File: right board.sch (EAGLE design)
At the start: 29 parts, among them IC1 LM555D, IC2 LM555D

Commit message: added switches to light board
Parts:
- added D2, D3, D6, D7: SRP100, diode:SRP100
- added U$1, U$2: JS_SERIES_SLIDESWITCCH, slide switch:JS_SERIES_SLIDESWITCCH
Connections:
- removed net N$13: C3.1, IC2.THR, VR2.S
- removed net N$17: VR2.E
- new net B_BLINK: IC1.GND, IC1.Q, NMOS.S, R3.2, U$1.OUT1
- new net D_BLINK: IC2.GND, IC2.Q, NMOS1.S, R6.2, U$2.OUT1
- new net N$1: D2.A, VR2.E
- new net N$9: D3.C, VR2.A
- net BLINK: now also U$1.IN; no longer IC1.GND, IC1.Q, NMOS.S, R3.2
- net B_OUT: now also U$1.OUT2
- net DRIVE: now also U$2.IN; no longer IC2.GND, IC2.Q, NMOS1.S, R6.2
- net D_OUT: now also U$2.OUT2
- net N$12: now also C1.1, IC1.R, IC1.THR, VR1.S; no longer IC2.DIS
- net N$14: now also D3.A, IC2.DIS; no longer VR2.A
- net N$18: now also D2.C
- net N$2: now also C3.1, IC2.R, IC2.THR, VR2.S; no longer IC1.DIS
- net N$3: now also D7.C, VR1.A; no longer C1.1, IC1.THR, VR1.S
- net N$4: now also D7.A, IC1.DIS; no longer VR1.A
- net N$5: now also D6.A
- net N$7: now also D6.C

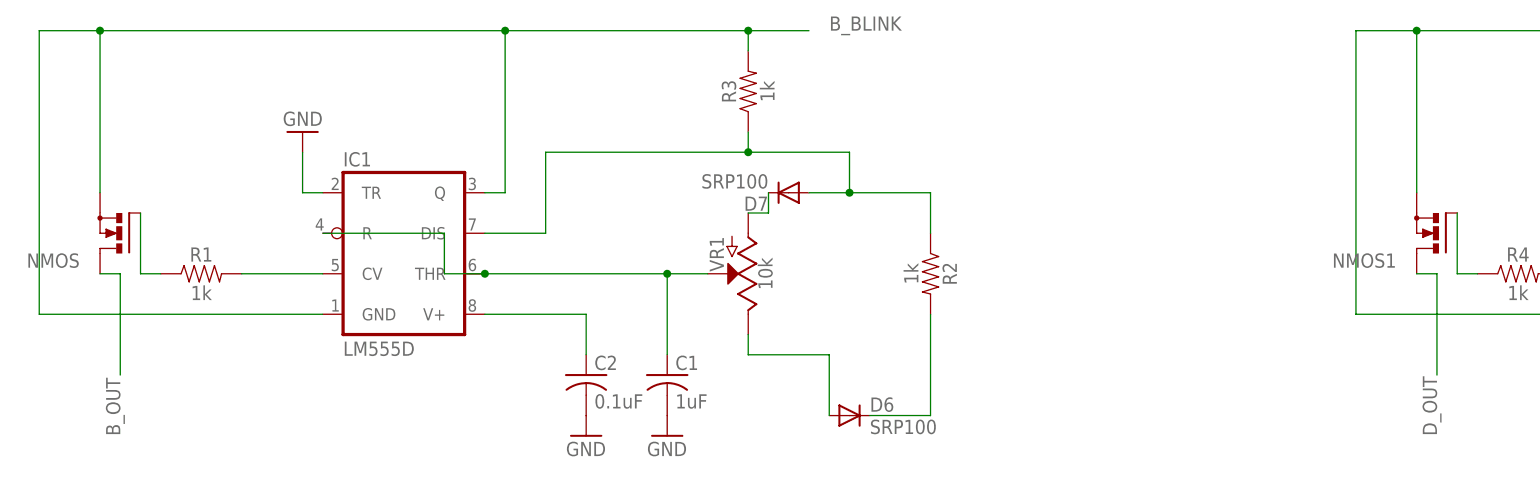
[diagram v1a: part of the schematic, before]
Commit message: updated mosfets on lights
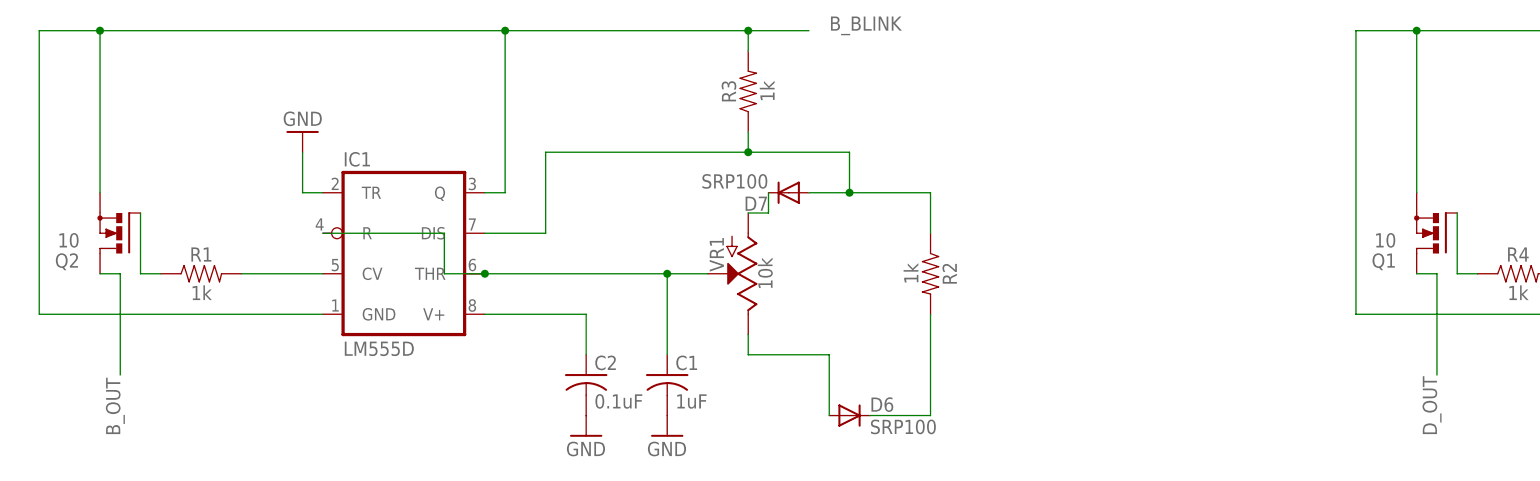
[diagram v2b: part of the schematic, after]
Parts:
- removed NMOS, NMOS1: (no value), transistor-power:N-MOSFET-SO8S
- added Q1, Q2: 10, transistor-power:PMOSFET_NTO220BV
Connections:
- net B_BLINK: now also Q2.S; no longer NMOS.S
- net B_OUT: now also Q2.D; no longer NMOS.D
- net D_BLINK: now also Q1.S; no longer NMOS1.S
- net D_OUT: now also Q1.D; no longer NMOS1.D
- net N$19: now also Q1.G; no longer NMOS1.G
- net N$8: now also Q2.G; no longer NMOS.G
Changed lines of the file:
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@@
 <part name="C2" library="E-P-008-R1.2" deviceset="C-US" device="025-024X044" value="0.1uF"/>
 <part name="GND1" library="E-P-008-R1.2" deviceset="GND" device=""/>
-<part name="NMOS" library="transistor-power" library_urn="urn:adsk.eagle:library:400" deviceset="N-MOSFET-SO8" device="S" package3d_urn="urn:adsk.eagle:package:29505/2"/>
 <part name="GND2" library="E-P-008-R1.2" deviceset="GND" device=""/>
 <part name="GND4" library="E-P-008-R1.2" deviceset="GND" device=""/>
@@
 <part name="C4" library="E-P-008-R1.2" deviceset="C-US" device="025-024X044" value="0.1uF"/>
 <part name="GND5" library="E-P-008-R1.2" deviceset="GND" device=""/>
-<part name="NMOS1" library="transistor-power" library_urn="urn:adsk.eagle:library:400" deviceset="N-MOSFET-SO8" device="S" package3d_urn="urn:adsk.eagle:package:29505/2"/>
 <part name="GND6" library="E-P-008-R1.2" deviceset="GND" device=""/>
 <part name="GND8" library="E-P-008-R1.2" deviceset="GND" device=""/>
@@
 <part name="D6" library="diode" library_urn="urn:adsk.eagle:library:210" deviceset="SRP100" device="" package3d_urn="urn:adsk.eagle:package:43336/1"/>
 <part name="D7" library="diode" library_urn="urn:adsk.eagle:library:210" deviceset="SRP100" device="" package3d_urn="urn:adsk.eagle:package:43336/1"/>
+<part name="Q1" library="transistor-power" library_urn="urn:adsk.eagle:library:400" deviceset="PMOSFET_N" device="TO220BV" package3d_urn="urn:adsk.eagle:package:29484/1" value="10"/>
+<part name="Q2" library="transistor-power" library_urn="urn:adsk.eagle:library:400" deviceset="PMOSFET_N" device="TO220BV" package3d_urn="urn:adsk.eagle:package:29484/1" value="10"/>
 </parts>
 <sheets>
@@
 <instance part="C2" gate="G$1" x="-66.04" y="25.4"/>
 <instance part="GND1" gate="1" x="-55.88" y="17.78"/>
-<instance part="NMOS" gate="G$1" x="-124.46" y="43.18" rot="R180"/>
 <instance part="GND2" gate="1" x="-66.04" y="17.78"/>
 <instance part="GND4" gate="1" x="-101.6" y="55.88" rot="R180"/>
@@
 <instance part="C4" gate="G$1" x="99.06" y="25.4"/>
 <instance part="GND5" gate="1" x="109.22" y="17.78"/>
-<instance part="NMOS1" gate="G$1" x="40.64" y="43.18" rot="R180"/>
 <instance part="GND6" gate="1" x="99.06" y="17.78"/>
 <instance part="GND8" gate="1" x="63.5" y="55.88" rot="R180"/>
@@
 <instance part="D6" gate="1" x="-33.02" y="20.32"/>
 <instance part="D7" gate="1" x="-40.64" y="48.26" rot="R180"/>
+<instance part="Q1" gate="G$1" x="40.64" y="43.18" rot="R180"/>
+<instance part="Q2" gate="G$1" x="-124.46" y="43.18" rot="R180"/>
 </instances>
 <busses>
@@
 <segment>
 <pinref part="R1" gate="G$1" pin="1"/>
-<pinref part="NMOS" gate="G$1" pin="G"/>
 <wire x1="-119.38" y1="38.1" x2="-121.92" y2="38.1" width="0.1524" layer="91"/>
 <wire x1="-121.92" y1="38.1" x2="-121.92" y2="45.72" width="0.1524" layer="91"/>
+<pinref part="Q2" gate="G$1" pin="G"/>
 </segment>
 </net>
@@
 <segment>
 <pinref part="R4" gate="G$1" pin="1"/>
-<pinref part="NMOS1" gate="G$1" pin="G"/>
 <wire x1="45.72" y1="38.1" x2="43.18" y2="38.1" width="0.1524" layer="91"/>
 <wire x1="43.18" y1="38.1" x2="43.18" y2="45.72" width="0.1524" layer="91"/>
+<pinref part="Q1" gate="G$1" pin="G"/>
 </segment>
 </net>
@@
 </segment>
 <segment>
-<pinref part="NMOS" gate="G$1" pin="D"/>
 <wire x1="-127" y1="38.1" x2="-124.46" y2="38.1" width="0.1524" layer="91"/>
 <wire x1="-124.46" y1="38.1" x2="-124.46" y2="25.4" width="0.1524" layer="91"/>
 <label x="-124.46" y="17.78" size="1.778" layer="95" rot="R90"/>
+<pinref part="Q2" gate="G$1" pin="D"/>
 </segment>
 <segment>
@@
 </segment>
 <segment>
-<pinref part="NMOS1" gate="G$1" pin="D"/>
 <wire x1="38.1" y1="38.1" x2="40.64" y2="38.1" width="0.1524" layer="91"/>
 <wire x1="40.64" y1="38.1" x2="40.64" y2="25.4" width="0.1524" layer="91"/>
 <label x="40.64" y="17.78" size="1.778" layer="95" rot="R90"/>
+<pinref part="Q1" gate="G$1" pin="D"/>
 </segment>
 <segment>
@@
 <wire x1="66.04" y1="33.02" x2="30.48" y2="33.02" width="0.1524" layer="91"/>
 <wire x1="30.48" y1="33.02" x2="30.48" y2="68.58" width="0.1524" layer="91"/>
-<pinref part="NMOS1" gate="G$1" pin="S"/>
 <wire x1="38.1" y1="48.26" x2="38.1" y2="68.58" width="0.1524" layer="91"/>
 <junction x="38.1" y="68.58"/>
@@
 <wire x1="119.38" y1="68.58" x2="119.38" y2="66.04" width="0.1524" layer="91"/>
 <junction x="119.38" y="68.58"/>
+<pinref part="Q1" gate="G$1" pin="S"/>
 </segment>
 </net>
@@
 <wire x1="-99.06" y1="33.02" x2="-134.62" y2="33.02" width="0.1524" layer="91"/>
 <wire x1="-134.62" y1="33.02" x2="-134.62" y2="68.58" width="0.1524" layer="91"/>
-<pinref part="NMOS" gate="G$1" pin="S"/>
 <wire x1="-127" y1="48.26" x2="-127" y2="68.58" width="0.1524" layer="91"/>
 <junction x="-127" y="68.58"/>
@@
 <wire x1="-45.72" y1="68.58" x2="-45.72" y2="66.04" width="0.1524" layer="91"/>
 <junction x="-45.72" y="68.58"/>
-</segment>
-</net>
+<pinref part="Q2" gate="G$1" pin="S"/>
+</segment>
+</net>

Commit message: Gerbers generated
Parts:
- removed C1, C3: 1uF, E-P-008-R1.2:C-US025-024X044
- removed C2, C4: 0.1uF, E-P-008-R1.2:C-US025-024X044
- removed D2, D3, D6, D7: SRP100, diode:SRP100
- removed LED30, LED31, LED32, LED33, LED34, LED35, LED36, LED37, LED38: (no value), E-P-008-R1.2:LED
- removed R1, R2, R3, R4, R5, R6: 1k, SparkFun-Resistors:1KOHM-0603-1/10W-1%
- removed VR1, VR2: 10k, SparkFun-Resistors:POTENTIOMETER-PTH-9MM-1/20W-20%
- added C5, C7: 1.0uF, SparkFun-Capacitors-extra:1.0UF-25V-+80/-20(0805)"
- added C6, C8: 0.1uF, SparkFun-Capacitors-extra:0.1UF-25V(+80/-20%)(0603)
- added D1, D10, D11, D12, D13, D14, D15, D16, D17, D18, D19, D20, D21, D22, D23, D24, D25, D26, D27, D28, D4, D5, D8, D9: (no value), SparkFun-LED:LED5MM
- added D29, D30, D31, D32: (no value), SparkFun-DiscreteSemi:DIODESMA
- added R10, R11, R13, R14, R9: 1k, SparkFun-Resistors:0.22OHM-1/4W-1%(0805)
- added R12: 30, SparkFun-Resistors:0.22OHM-1/4W-1%(0805)
- added U$3: 10k, SparkFun-Resistors:10K_LINEAR_POT_SMD
- added U$4: 10K_LINEAR_POT_SMD, SparkFun-Resistors:10K_LINEAR_POT_SMD
- R7: value (none) -> 30; device resistor:R-US_0204/2V -> SparkFun-Resistors:0.22OHM-1/4W-1%(0805)
- R8: value (none) -> 1k; device resistor:R-US_0204/5 -> SparkFun-Resistors:0.22OHM-1/4W-1%(0805)
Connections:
- removed net N$37: LED30.C, LED31.A
- removed net N$38: LED31.C, LED32.A
- removed net N$39: LED32.C, LED33.A
- removed net N$40: LED34.C, LED35.A
- removed net N$41: LED35.C, LED36.A
- removed net N$42: LED36.C, LED37.A
- removed net N$43: LED30.A, R8.2
- removed net N$44: LED34.A, R7.1
- removed net N$48: LED37.C, LED38.A
- new net N$11: D1.C, D10.A, D11.A, D12.A, D4.C, D5.C, D8.C, D9.A
- new net N$13: D1.A, D4.A, D5.A, D8.A, R12.2
- new net N$17: D17.C, D18.C, D19.C, D20.C, D21.A, D22.A, D23.A, D24.A
- new net N$20: D21.C, D22.C, D23.C, D24.C, D25.A, D26.A, D27.A, D28.A
- new net N$21: D10.C, D11.C, D12.C, D13.A, D14.A, D15.A, D16.A, D9.C
- new net N$22: D17.A, D18.A, D19.A, D20.A, R7.2
- net B_BLINK: now also R13.2; no longer R3.2
- net B_OUT: now also R12.1; no longer R8.1
- net D_BLINK: now also R9.1; no longer R6.2
- net D_OUT: now also R7.1; no longer R7.2
- net GND: now also C5.2, C6.2, C7.2, C8.2, D13.C, D14.C, D15.C, D16.C, D25.C, D26.C, D27.C, D28.C; no longer C1.2, C2.2, C3.2, C4.2, LED33.C, LED38.C
- net N$1: now also D29.A, U$4.E; no longer D2.A, VR2.E
- net N$10: now also R14.1; no longer R1.2
- net N$12: now also C7.1, U$3.S; no longer C1.1, VR1.S
- net N$14: now also D30.A, R8.1, R9.2; no longer D3.A, R5.1, R6.1
- net N$15: now also C6.1; no longer C4.1
- net N$16: now also R10.2; no longer R4.2
- net N$18: now also D29.C, R8.2; no longer D2.C, R5.2
- net N$19: now also R10.1; no longer R4.1
- net N$2: now also C5.1, U$4.S; no longer C3.1, VR2.S
- net N$3: now also D32.C, U$3.A; no longer D7.C, VR1.A
- net N$4: now also D32.A, R11.2, R13.1; no longer D7.A, R2.1, R3.1
- net N$5: now also D31.A, U$3.E; no longer D6.A, VR1.E
- net N$6: now also C8.1; no longer C2.1
- net N$7: now also D31.C, R11.1; no longer D6.C, R2.2
- net N$8: now also R14.2; no longer R1.1
- net N$9: now also D30.C, U$4.A; no longer D3.C, VR2.A
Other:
- moved on the sheet: R7, R8

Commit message: all gerbers generated
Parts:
- added H1, H2, H3, H4: STAND-OFF, SparkFun-Electromechanical:STAND-OFF
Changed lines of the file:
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@@
 <part name="C7" library="SparkFun-Capacitors-extra" deviceset="1.0UF-25V-+80/-20(0805)" device="&quot;" value="1.0uF"/>
 <part name="C8" library="SparkFun-Capacitors-extra" deviceset="0.1UF-25V(+80/-20%)(0603)" device="" value="0.1uF"/>
+<part name="H1" library="SparkFun-Electromechanical" deviceset="STAND-OFF" device=""/>
+<part name="H2" library="SparkFun-Electromechanical" deviceset="STAND-OFF" device=""/>
+<part name="H3" library="SparkFun-Electromechanical" deviceset="STAND-OFF" device=""/>
+<part name="H4" library="SparkFun-Electromechanical" deviceset="STAND-OFF" device=""/>
 </parts>
 <sheets>
@@
 <instance part="C7" gate="G$1" x="-55.88" y="22.86"/>
 <instance part="C8" gate="G$1" x="-66.04" y="22.86"/>
+<instance part="H1" gate="G$1" x="71.12" y="86.36"/>
+<instance part="H2" gate="G$1" x="76.2" y="86.36"/>
+<instance part="H3" gate="G$1" x="81.28" y="86.36"/>
+<instance part="H4" gate="G$1" x="86.36" y="86.36"/>
 </instances>
 <busses>

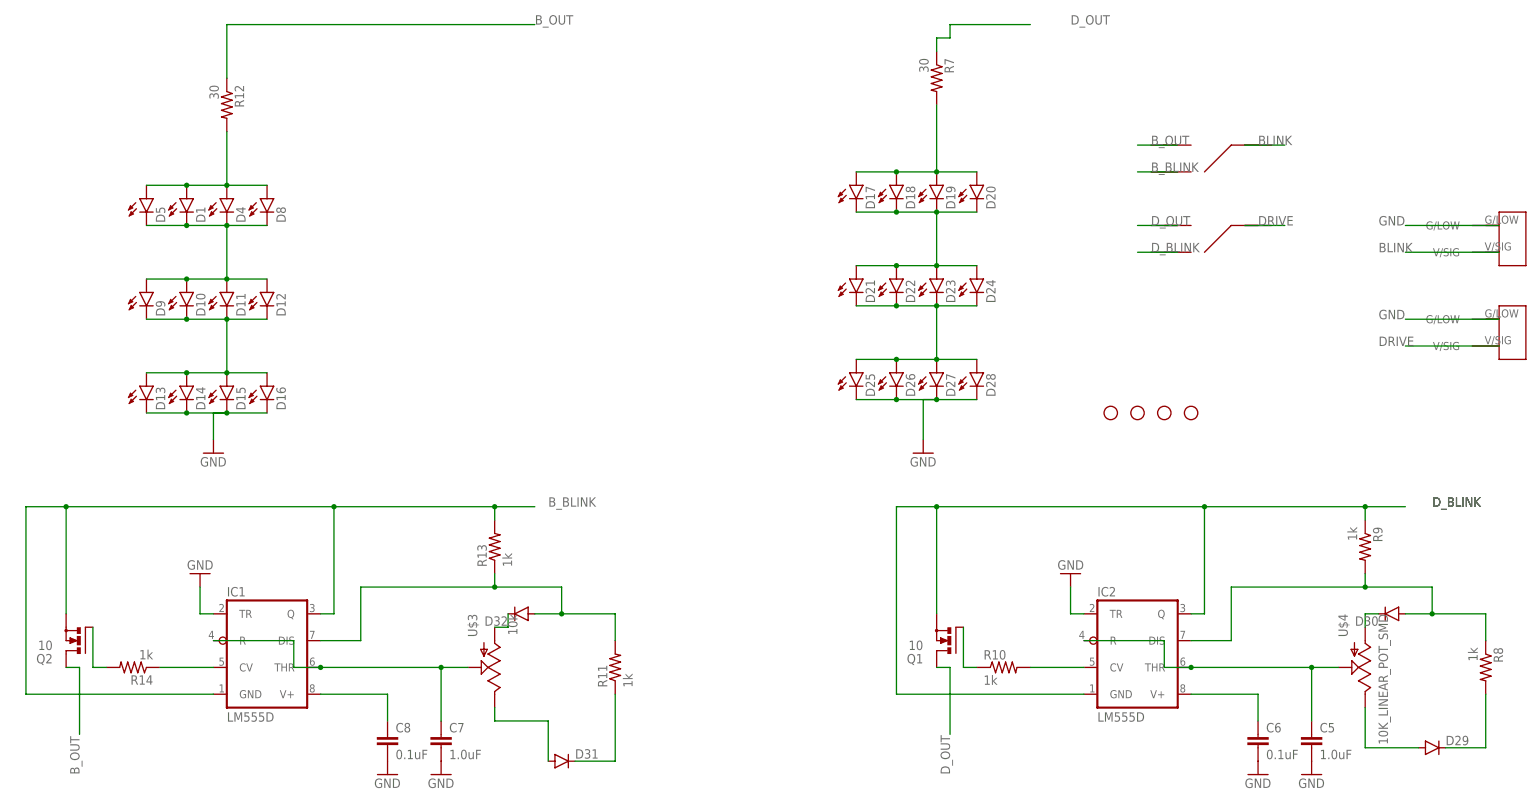
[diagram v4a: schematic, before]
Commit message: added reverse polairity protection
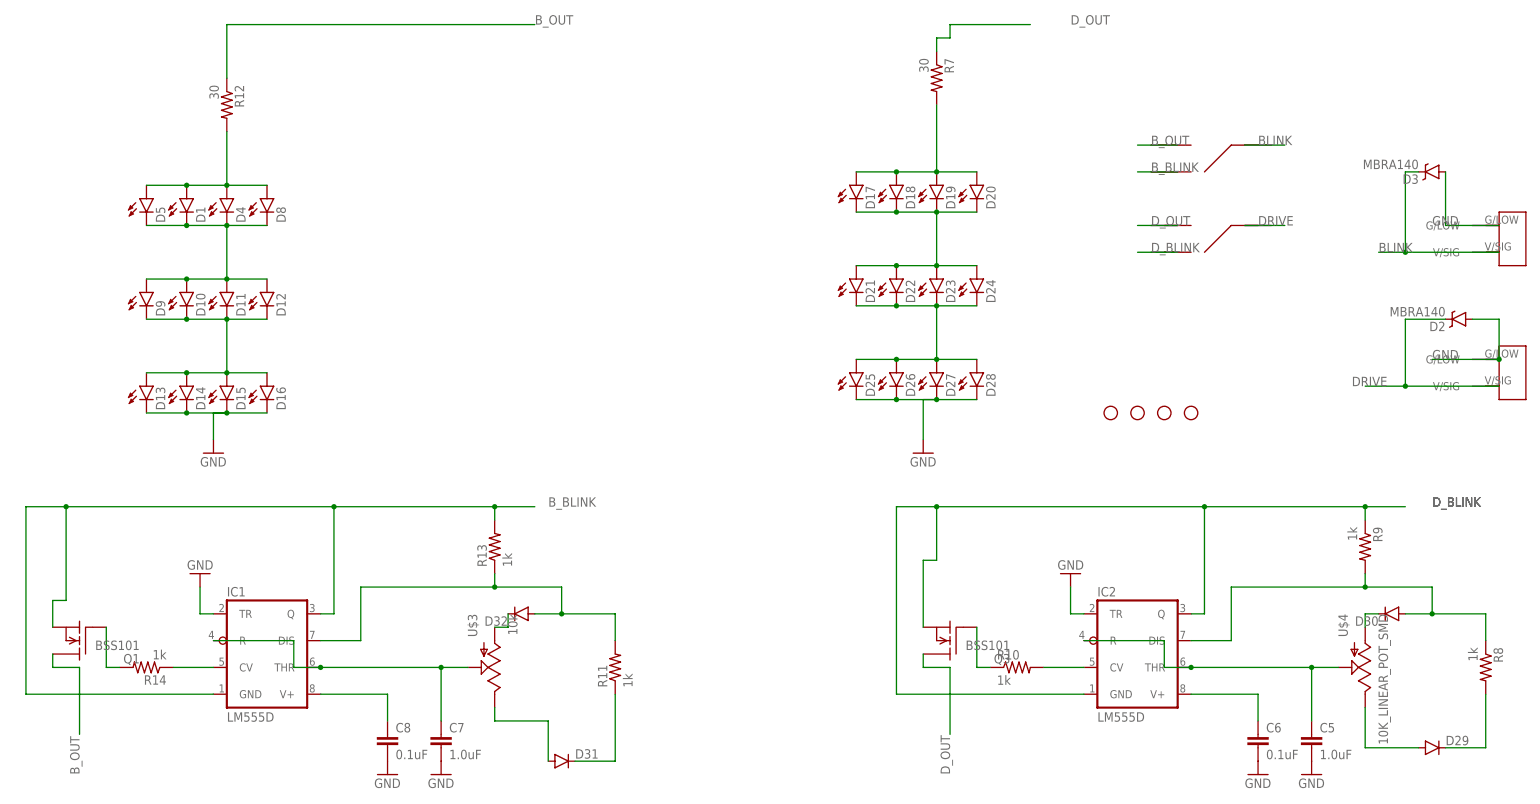
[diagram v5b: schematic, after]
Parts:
- removed Q2: 10, transistor-power:PMOSFET_NTO220BV
- removed R_DRIVE: 2_PIN_TECONNECTOR, TE 2-pin connector:2_PIN_TECONNECTOR
- added D2, D3: MBRA140, SparkFun-DiscreteSemi:MBRA140
- added Q3: BSS101, transistor-fet:BSS101
- added U$6: 2_PIN_TECONNECTOR, TE 2-pin connector:2_PIN_TECONNECTOR
- Q1: value 10 -> BSS101; device transistor-power:PMOSFET_NTO220BV -> transistor-fet:BSS101
- renumbered R_BLINK to U$5
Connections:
- net BLINK: now also D3.C
- net B_BLINK: now also Q1.S; no longer Q2.S
- net B_OUT: now also Q1.D; no longer Q2.D
- net DRIVE: now also D2.C, U$6.V/SIG; no longer R_DRIVE.V/SIG
- net D_BLINK: now also Q3.S; no longer Q1.S
- net D_OUT: now also Q3.D; no longer Q1.D
- net GND: now also D2.A, D3.A, U$6.G/LOW; no longer R_DRIVE.G/LOW
- net N$19: now also Q3.G; no longer Q1.G
- net N$8: now also Q1.G; no longer Q2.G
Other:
- moved on the sheet: R10, R14
